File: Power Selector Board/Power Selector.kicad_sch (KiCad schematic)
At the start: 11 parts, among them J101 MSD-DB01M-12P, J102 MSD-DB01F-12P_1, J103 64900221122, J104 64900221122, J105 64900221122, K101 G6SK-2G DC24, U101 1720466

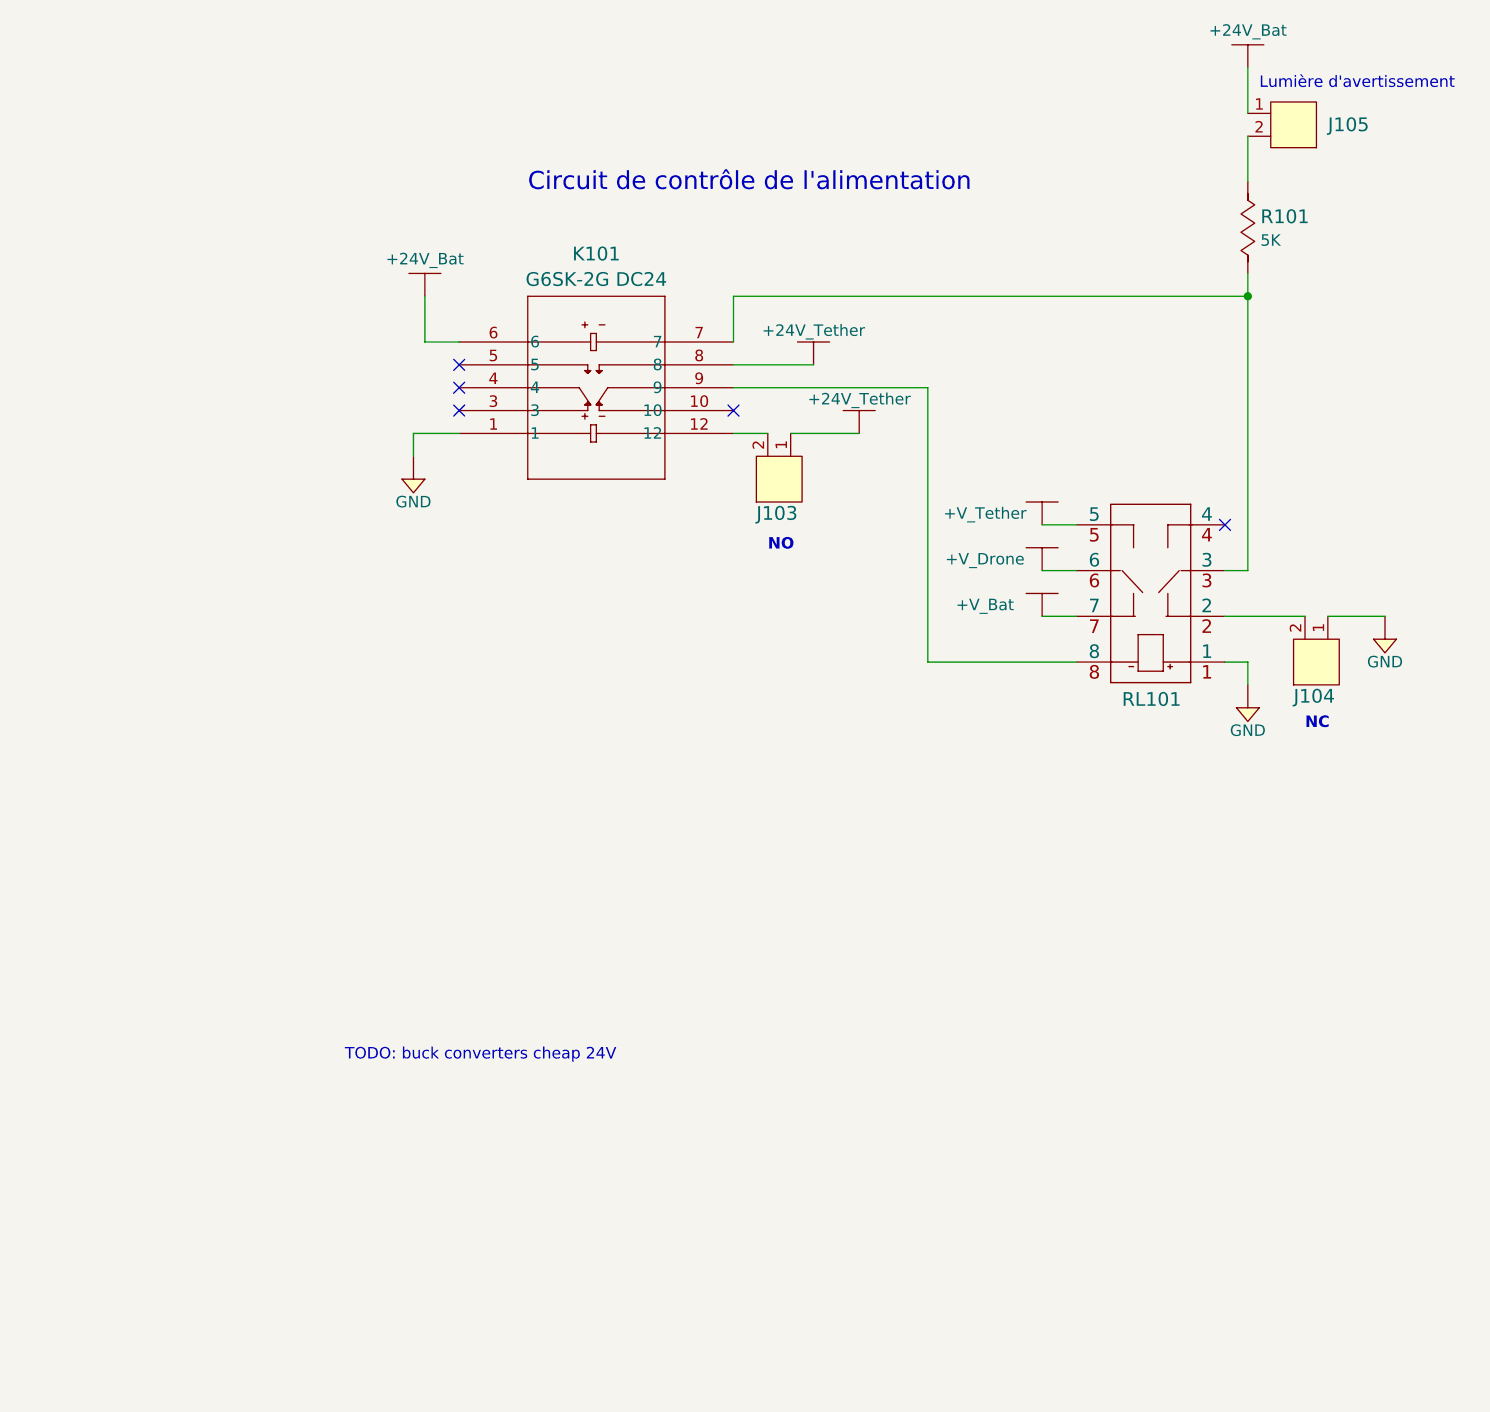
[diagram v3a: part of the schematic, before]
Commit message: Ajout du circuit de la tension de controle
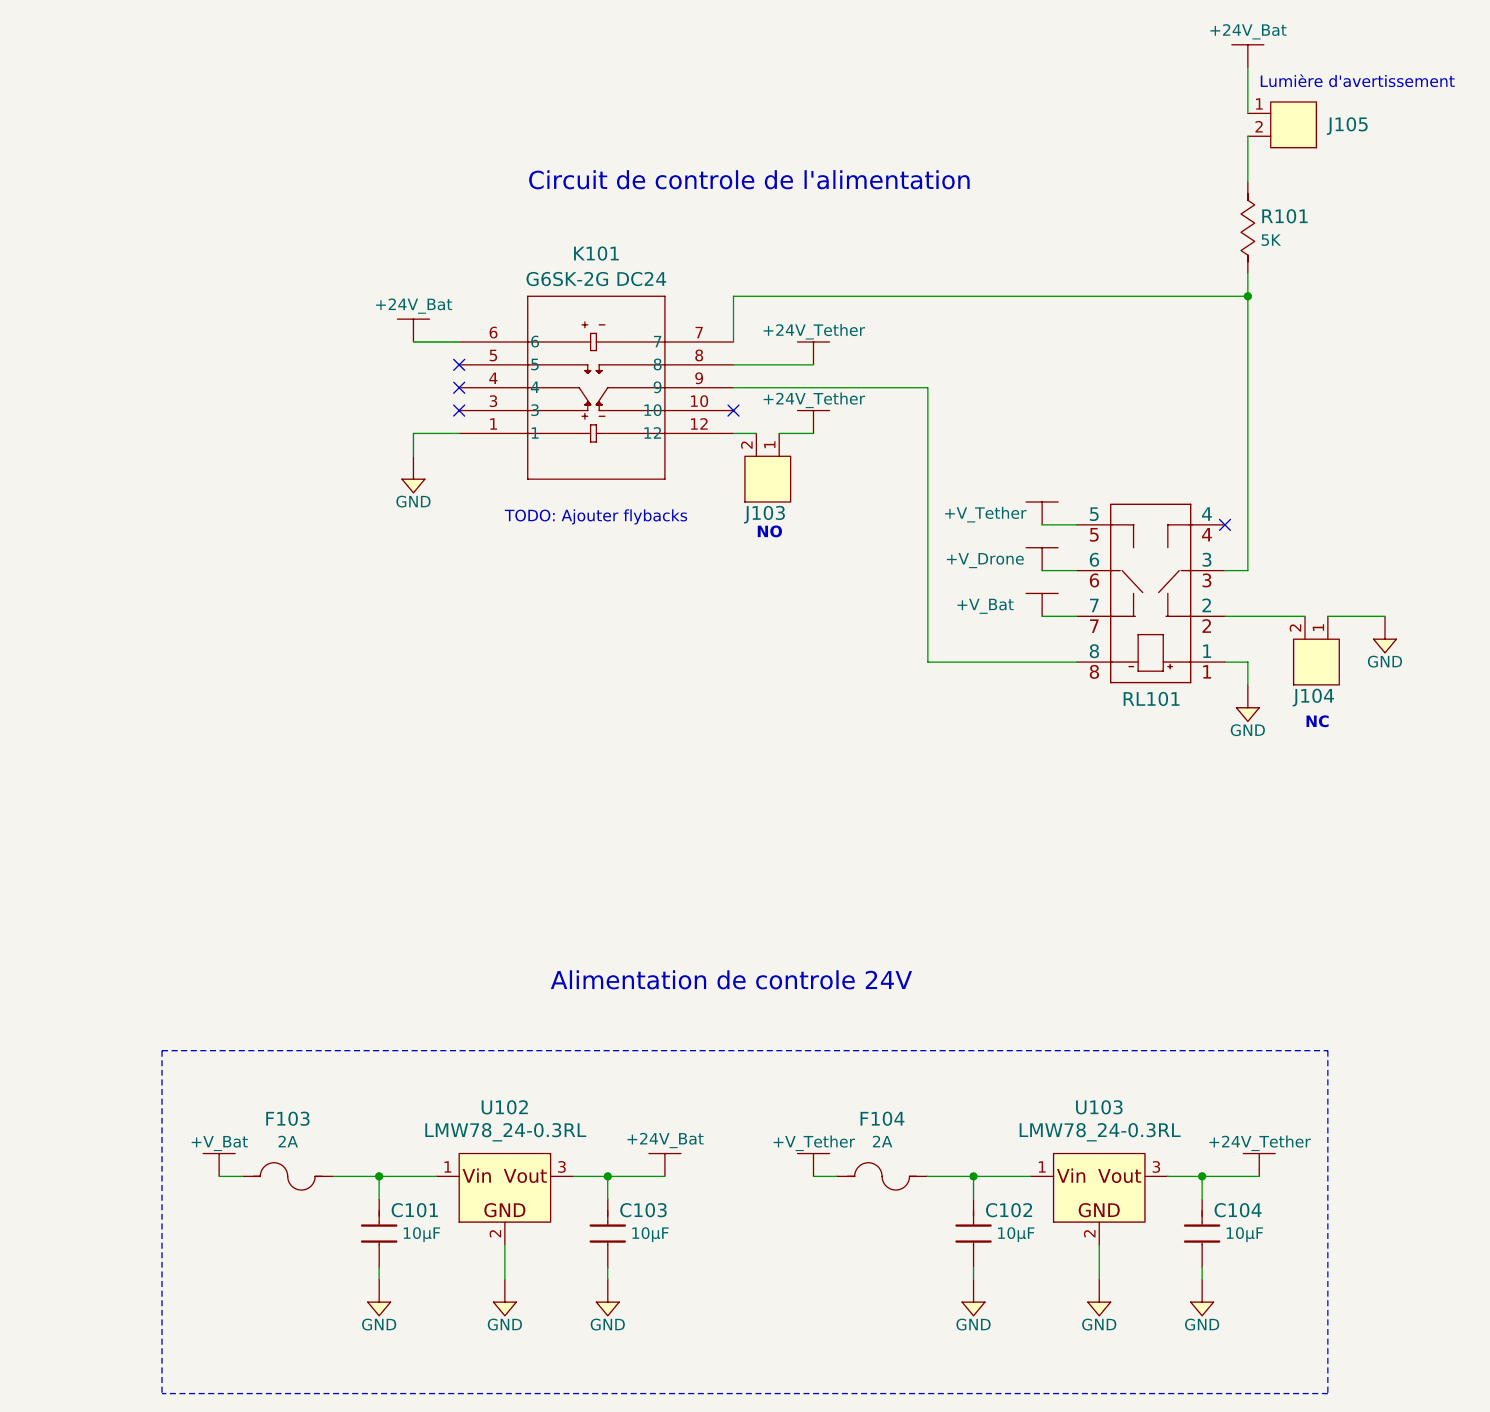
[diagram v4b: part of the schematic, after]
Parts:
- added C101, C102, C103, C104: GRM32EC72A106ME05L, Capacitors:C1210, symbol Capacitors:GRM32EC72A106ME05L
- added F103, F104: 0698Q2000-02, Fuses:TE5_395, symbol Fuses:0698Q2000-02
- added U102, U103: LMW78_24-0.3RL, Assembly:OKI-78SR_Horizontal, symbol PMIC:LMW78_24-0.3RL
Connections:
- net +VBat: now also F103.1, F104.1
- net 24V: now also C103.2, C104.2, U102.3 (Vout), U103.3 (Vout)
- net GND: now also C101.1, C102.1, C103.1, C104.1, U102.2 (GND), U103.2 (GND)
- new net: C102.2, F104.2, U103.1 (Vin)
- new net: C101.2, F103.2, U102.1 (Vin)
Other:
- note added: "Alimentation de controle 24V"
- note added: "Circuit de controle de l'alimentation"
- note added: "TODO: Ajouter flybacks"
- note removed: "Circuit de contrôle de l'alimentation"
- note removed: "TODO: buck converters cheap 24V"

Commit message: Finalisation du schema, en atttente d'un design review, PCB pret a commencer a etre routé
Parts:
- removed RL101: 2-1462039-9, Relays:2-1462039-9, symbol Relays:2-1462039-9
- added D101, D102, D103: S1D-13-F, Diodes:SMA_DIO, symbol Diodes:S1D-13-F
- added K102, K103: J115F11C24VDCSH.9, RELAY5_J115F11C24VDCSH.9_CRS, symbol Relays:J115F11C24VDCSH.9
- F101, F102: Current Rating (A) 24A -> 30A
- R101: Resistance (Ohms) 5K -> 120
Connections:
- net GND: now also J104.2, K101.12, D101.2, D102.2, D103.2, K102.5, K103.5; no longer J104.1, K101.1
- net at K101.7, R101.1: now also K103.1
- net at J103.2: now also K101.1, D103.1; no longer K101.12
- net Relay_Active: now reaches K101.9
- net Relay_Active: now also D101.1, D102.1, K102.4, K103.4
- net +V_Drone: now reaches J101.1, J101.2, J101.3, J101.4, J101.5
- net +V_Drone: now also F101.1, F104.1, K102.2, K102.3; no longer F102.~
- net at U101.1, U101.2, U101.3: now also F101.2; no longer F101.~
- net +VBat: no longer names the net of J102.1, J102.2, J102.3, J102.4, J102.5
- net +VBat: now also F102.2; no longer F101.~, F102.~, F103.1, F104.1
- net 24V renamed 24V_Bat
- net 24V_Bat: no longer C104.2, J103.1, K101.8, U103.3 (Vout)
- new net: J104.1, K103.3
- new net +V_Bat: F102.1, F103.1, K102.1
- new net 24V_Tether: C104.2, J103.1, K101.8, U103.3 (Vout)
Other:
- note added: "NC Bouton"
- note added: "NO Bouton"
- note added: "NOTE: Les fuses peuvent être shortées après que les tests soient conclus: une fuse qui lâche en plein vol causera fort probablement une perte du drone"
- note removed: "NC"
- note removed: "NO"
- note removed: "TODO: Ajouter flybacks"
- moved on the sheet: C101, C102, C103, C104, F103, F104, J101, J102, J104, J105, R101, U101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

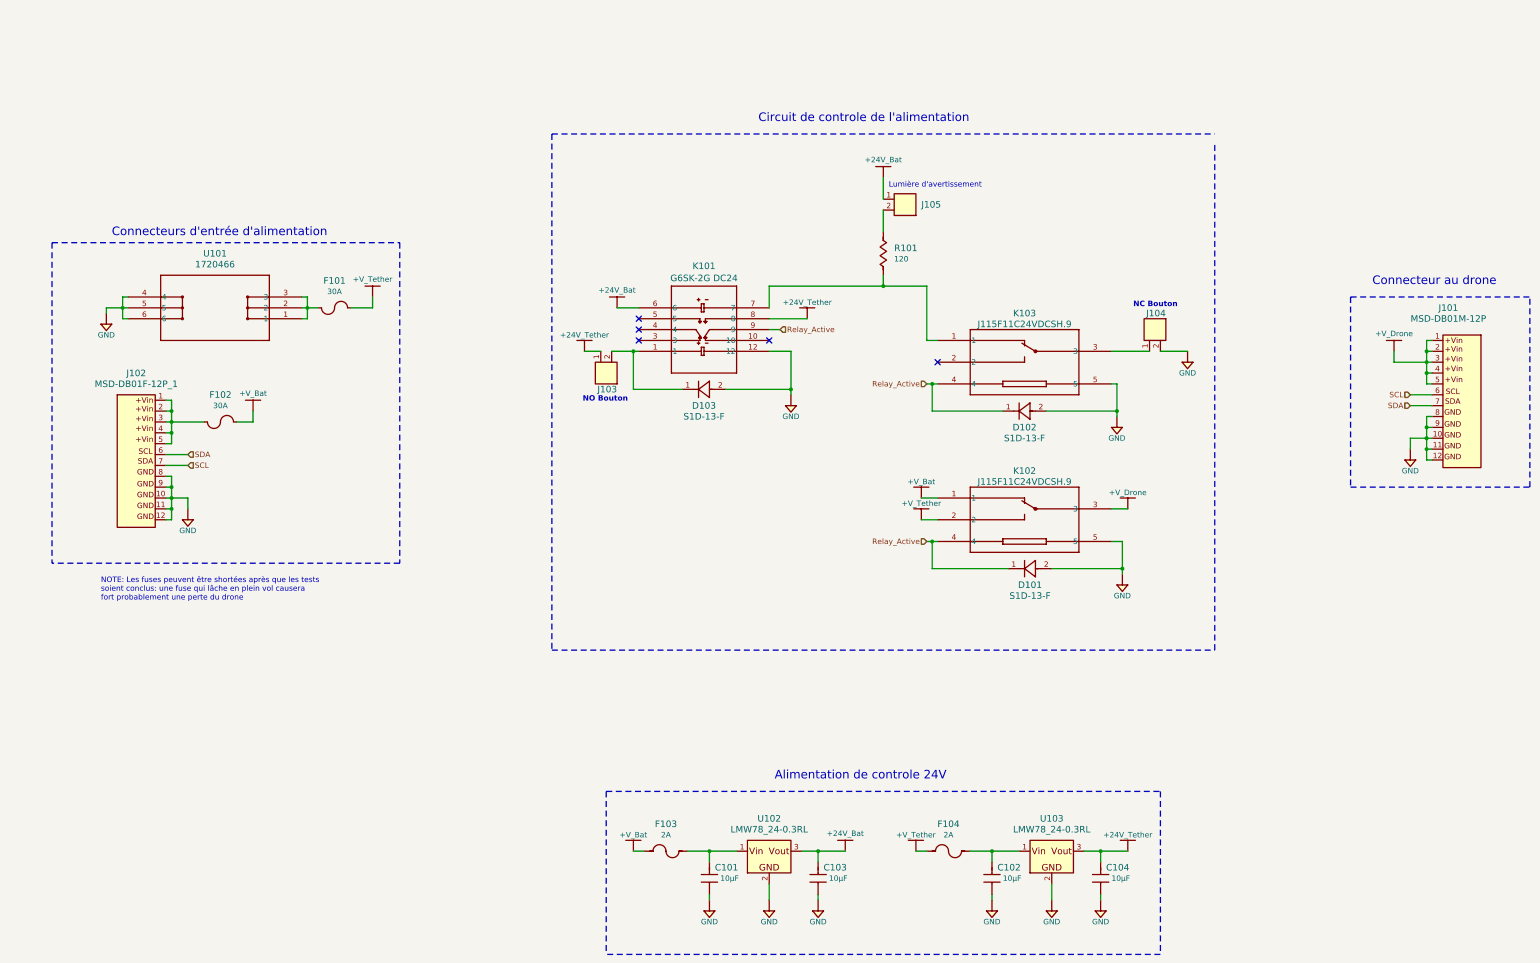
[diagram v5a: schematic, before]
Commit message: Debut routing
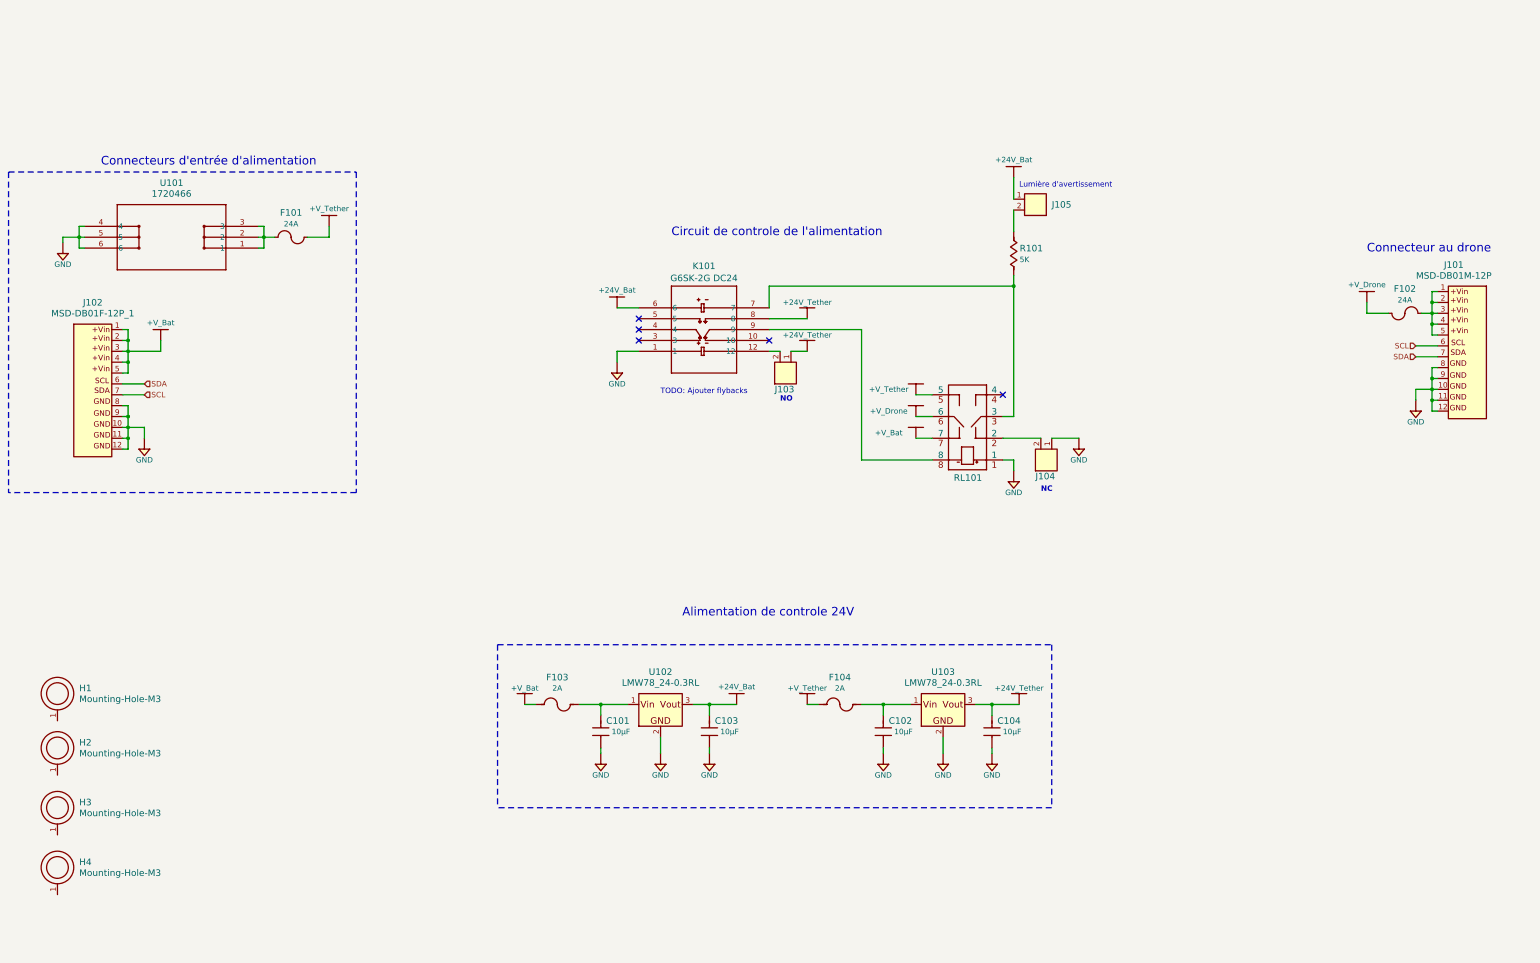
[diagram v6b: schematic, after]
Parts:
- removed D101, D102, D103: S1D-13-F, Diodes:SMA_DIO, symbol Diodes:S1D-13-F
- removed K102, K103: J115F11C24VDCSH.9, RELAY5_J115F11C24VDCSH.9_CRS, symbol Relays:J115F11C24VDCSH.9
- added H1, H2, H3, H4: Mounting-Hole-M3, Connectors:Mounting_Hole_3mm, symbol Mechanicals:Mounting-Hole-M3
- added RL101: 2-1462039-9, Relays:2-1462039-9, symbol Relays:2-1462039-9
- F101, F102: Current Rating (A) 30A -> 24A
- J101, J102: footprint Connectors:649012227222 -> Connectors:MSD-DB01F-12P-V2.0
- R101: Resistance (Ohms) 120 -> 5K
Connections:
- net 24V_Tether is gone; now on net 24V: C104.2, J103.1, K101.8, U103.3 (Vout)
- net GND: now also J104.1, K101.1, RL101.1; no longer J104.2, K101.12
- net at K101.7, R101.1: now also RL101.3
- net at J103.2: now also K101.12; no longer K101.1
- net +VBat: now reaches J102.1, J102.2, J102.3, J102.4, J102.5
- net +VBat: now also F101.~, F102.~, F103.1, F104.1, RL101.5, RL101.6, RL101.7; no longer F102.2
- net at U101.1, U101.2, U101.3: now also F101.~; no longer F101.2
- removed net +V_Bat: F102.1, F103.1
- net +V_Drone: no longer names the net of J101.1, J101.2, J101.3, J101.4, J101.5
- net +V_Drone: now also F102.~; no longer F101.1, F104.1
- net 24V_Bat renamed 24V
- net Relay_Active: no longer names the net of K101.9
- net Relay_Active: now also RL101.8
- new net: J104.2, RL101.2
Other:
- note added: "NC"
- note added: "NO"
- note added: "TODO: Ajouter flybacks"
- note removed: "NC Bouton"
- note removed: "NO Bouton"
- note removed: "NOTE: Les fuses peuvent être shortées après que les tests soient conclus: une fuse qui lâche en plein vol causera fort probablement une perte du drone"
- moved on the sheet: C101, C102, C103, C104, F103, F104, J101, J102, J104, J105, R101, U101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

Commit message: Fix du bug github, devrait etre la bonne version
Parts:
- removed H1, H2, H3, H4: Mounting-Hole-M3, Connectors:Mounting_Hole_3mm, symbol Mechanicals:Mounting-Hole-M3
- removed RL101: 2-1462039-9, Relays:2-1462039-9, symbol Relays:2-1462039-9
- added D101, D102, D103: S1D-13-F, Diodes:SMA_DIO, symbol Diodes:S1D-13-F
- added K102, K103: J115F11C24VDCSH.9, RELAY5_J115F11C24VDCSH.9_CRS, symbol Relays:J115F11C24VDCSH.9
- F101, F102: Current Rating (A) 24A -> 30A
- J101, J102: footprint Connectors:MSD-DB01F-12P-V2.0 -> Connectors:649012227222
- R101: Resistance (Ohms) 5K -> 120
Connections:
- net GND: now also J104.2, K101.12, D101.2, D102.2, D103.2, K102.5, K103.5; no longer J104.1, K101.1
- net at K101.7, R101.1: now also K103.1
- net at J103.2: now also K101.1, D103.1; no longer K101.12
- net Relay_Active: now reaches K101.9
- net Relay_Active: now also D101.1, D102.1, K102.4, K103.4
- net +V_Drone: now reaches J101.1, J101.2, J101.3, J101.4, J101.5
- net +V_Drone: now also F101.1, F104.1, K102.2, K102.3; no longer F102.~
- net at U101.1, U101.2, U101.3: now also F101.2; no longer F101.~
- net +VBat: no longer names the net of J102.1, J102.2, J102.3, J102.4, J102.5
- net +VBat: now also F102.2; no longer F101.~, F102.~, F103.1, F104.1
- net 24V renamed 24V_Bat
- net 24V_Bat: no longer C104.2, J103.1, K101.8, U103.3 (Vout)
- new net: J104.1, K103.3
- new net +V_Bat: F102.1, F103.1, K102.1
- new net 24V_Tether: C104.2, J103.1, K101.8, U103.3 (Vout)
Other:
- note added: "NC Bouton"
- note added: "NO Bouton"
- note added: "NOTE: Les fuses peuvent être shortées après que les tests soient conclus: une fuse qui lâche en plein vol causera fort probablement une perte du drone"
- note removed: "NC"
- note removed: "NO"
- note removed: "TODO: Ajouter flybacks"
- moved on the sheet: C101, C102, C103, C104, F103, F104, J101, J102, J104, J105, R101, U101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
